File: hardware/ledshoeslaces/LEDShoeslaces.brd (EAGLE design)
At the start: 50 x 38 mm, 13 parts, among them IC1 LM1117MPX-5.0

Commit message: fix button....
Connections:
- net GND: now also S1.3
- net VCC: no longer S1.3
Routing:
- net VCC: track 44.5 -> 36.0 mm

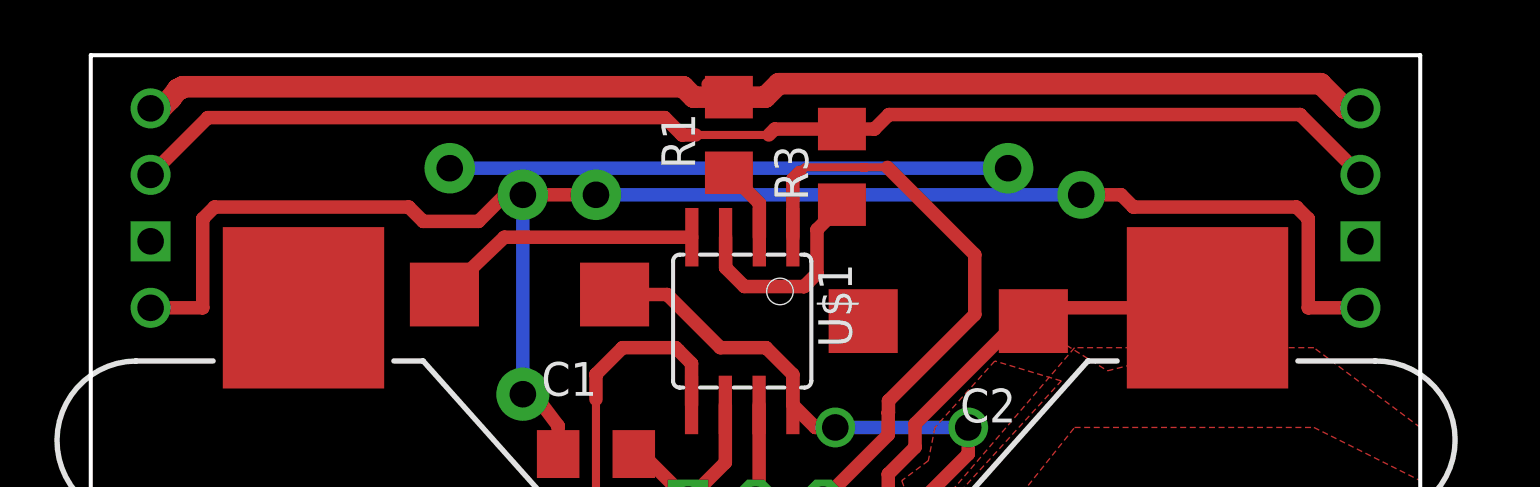
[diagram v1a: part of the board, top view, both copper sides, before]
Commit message: led pad size
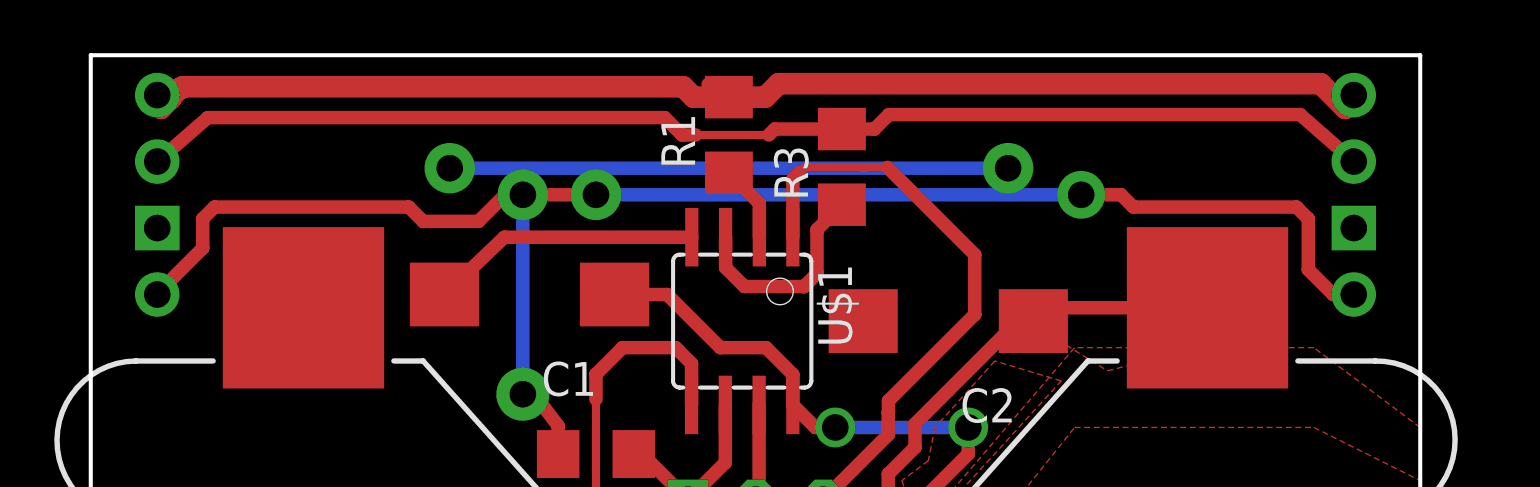
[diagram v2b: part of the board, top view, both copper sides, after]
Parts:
- moved U$3 0.56 mm to (2.50, 33.0)
- moved U$4 0.56 mm to (47.5, 33.0)
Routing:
- net ARED: track 64.5 -> 61.5 mm
- net AGRN: track 47.9 -> 46.9 mm
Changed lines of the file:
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@@
 <element name="C1" library="rcl" library_urn="urn:adsk.eagle:library:334" package="CT7343" package3d_urn="urn:adsk.eagle:package:23304/1" value="" x="16.5" y="29" rot="R180"/>
 <element name="C2" library="rcl" library_urn="urn:adsk.eagle:library:334" package="CT7343" package3d_urn="urn:adsk.eagle:package:23304/1" value="" x="32.25" y="28" rot="R180"/>
-<element name="U$3" library="fab" package="LEDRGB" value="LEDRGB" x="2.25" y="32.5" rot="R90"/>
-<element name="U$4" library="fab" package="LEDRGB" value="LEDRGB" x="47.75" y="32.5" rot="R90"/>
+<element name="U$3" library="fab" package="LEDRGB" value="LEDRGB" x="2.5" y="33" rot="R90"/>
+<element name="U$4" library="fab" package="LEDRGB" value="LEDRGB" x="47.5" y="33" rot="R90"/>
 </elements>
 <signals>
@@
 <wire x1="25.36603125" y1="36.422" x2="25.87243125" y2="36.9284" width="0.8128" layer="1"/>
 <wire x1="46.254125" y1="36.9284" x2="25.87243125" y2="36.9284" width="0.8128" layer="1"/>
-<wire x1="47.75" y1="36" x2="47.182525" y2="36" width="0.8128" layer="1"/>
+<wire x1="47.5" y1="36.5" x2="47.182525" y2="36" width="0.8128" layer="1"/>
 <wire x1="47.182525" y1="36" x2="46.254125" y2="36.9284" width="0.8128" layer="1"/>
 <wire x1="3.00575" y1="36.36233125" x2="3.27603125" y2="36.72270625" width="0.8128" layer="1"/>
 <wire x1="3.27603125" y1="36.72270625" x2="3.381140625" y2="36.737721875" width="0.8128" layer="1"/>
 <wire x1="3.381140625" y1="36.737721875" x2="3.45621875" y2="36.8128" width="0.8128" layer="1"/>
-<wire x1="2.25" y1="36" x2="2.64341875" y2="36" width="0.8128" layer="1"/>
+<wire x1="2.5" y1="36.5" x2="2.64341875" y2="36" width="0.8128" layer="1"/>
 <wire x1="2.64341875" y1="36" x2="3.00575" y2="36.36233125" width="0.8128" layer="1"/>
 <wire x1="3.45621875" y1="36.8128" x2="22.28125" y2="36.8128" width="0.8128" layer="1"/>
@@
 <contactref element="U$4" pad="1"/>
 <wire x1="16.329640625" y1="25.717425" x2="16.25" y2="25.25" width="0.508" layer="1"/>
-<wire x1="2.25" y1="28.5" x2="4.211" y2="28.5" width="0.508" layer="1"/>
-<wire x1="4.211" y1="28.5" x2="4.211" y2="31.84731875" width="0.508" layer="1"/>
+<wire x1="4.211" y1="30.744678125" x2="4.211" y2="31.84731875" width="0.508" layer="1"/>
 <wire x1="4.211" y1="31.84731875" x2="4.65268125" y2="32.289" width="0.508" layer="1"/>
 <wire x1="15.5834" y1="32.75" x2="16.25" y2="32.75" width="0.508" layer="1"/>
 <wire x1="38.75" y1="32.75" x2="37.25" y2="32.75" width="0.508" layer="1"/>
-<wire x1="47.75" y1="28.5" x2="45.789" y2="28.5" width="0.508" layer="1"/>
-<wire x1="45.789" y1="28.5" x2="45.789" y2="31.84731875" width="0.508" layer="1"/>
+<wire x1="45.789" y1="29.93560625" x2="45.789" y2="31.84731875" width="0.508" layer="1"/>
 <wire x1="45.789" y1="31.84731875" x2="45.34731875" y2="32.289" width="0.508" layer="1"/>
 <wire x1="45.34731875" y1="32.289" x2="39.211" y2="32.289" width="0.508" layer="1"/>
@@
 <wire x1="17.578" y1="23" x2="17.578" y2="24.059784375" width="0.508" layer="1"/>
 <wire x1="17.578" y1="24.059784375" x2="16.329640625" y2="25.717425" width="0.508" layer="1"/>
+<wire x1="47.5" y1="29" x2="46.72460625" y2="29" width="0.508" layer="1"/>
+<wire x1="46.72460625" y1="29" x2="45.789" y2="29.93560625" width="0.508" layer="1"/>
+<wire x1="2.5" y1="29" x2="2.466321875" y2="29" width="0.508" layer="1"/>
+<wire x1="2.466321875" y1="29" x2="4.211" y2="30.744678125" width="0.508" layer="1"/>
 </signal>
 <signal name="AGRN">
@@
 <wire x1="25.722" y1="35.222" x2="25.5" y2="35" width="0.508" layer="1"/>
 <wire x1="28.25" y1="35.222" x2="29.472" y2="35.222" width="0.508" layer="1"/>
-<wire x1="29.472" y1="35.222" x2="30.018" y2="35.768" width="0.508" layer="1"/>
+<wire x1="30.018" y1="35.768" x2="29.472" y2="35.222" width="0.508" layer="1"/>
 <wire x1="30.018" y1="35.768" x2="45.482" y2="35.768" width="0.508" layer="1"/>
-<wire x1="45.482" y1="35.768" x2="47.75" y2="33.5" width="0.508" layer="1"/>
+<wire x1="45.482" y1="35.768" x2="47.5" y2="34" width="0.508" layer="1"/>
 <wire x1="22.23746875" y1="35" x2="22.75" y2="35" width="0.508" layer="1"/>
-<wire x1="2.25" y1="33.5" x2="4.4024" y2="35.6524" width="0.508" layer="1"/>
+<wire x1="2.5" y1="34" x2="4.4024" y2="35.6524" width="0.508" layer="1"/>
 <wire x1="4.4024" y1="35.6524" x2="21.58506875" y2="35.6524" width="0.508" layer="1"/>
 <wire x1="21.58506875" y1="35.6524" x2="22.23746875" y2="35" width="0.508" layer="1"/>
